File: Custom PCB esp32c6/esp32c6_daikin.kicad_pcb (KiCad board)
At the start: 2 copper layers, 31.6 x 19.8 mm, 31 parts, among them J2 Conn_01x07, Q1 BSS138PS, U1 TPS562246, U2 WT0132C6-S5

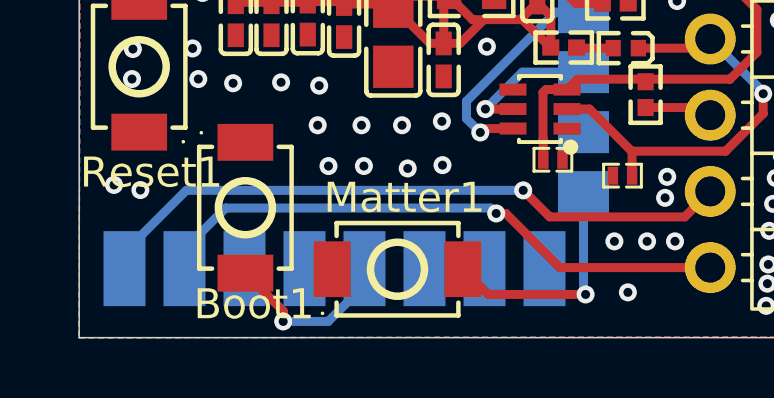
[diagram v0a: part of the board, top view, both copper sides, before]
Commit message: fix(pcb): move Boot1 via clear of the board edge
Sat 0.24mm from Edge.Cuts against a 0.5mm rule; edge routing tolerance
could nick it. A plain perpendicular retreat wasn't viable: the via sits
in a 1.05mm corridor between the U2 castellated pad row (0.6mm gaps
between 2.0mm-pitch pads) and the board edge, too tight to gain edge
clearance without shorting an adjacent pad. Relocated it into the same-net
column under U2 pad 12 (161.4,109.03 -> 164.11,108.6) and re-terminated
the two connected track segments there instead.

Also hardened refill.py to disable wx assert dialogs (wx.DisableAsserts())
so a stray pcbnew API nag (PCB_VIA::GetWidth called without a layer
argument, hit while probing pad geometry for this fix) can't block
future headless refill runs.
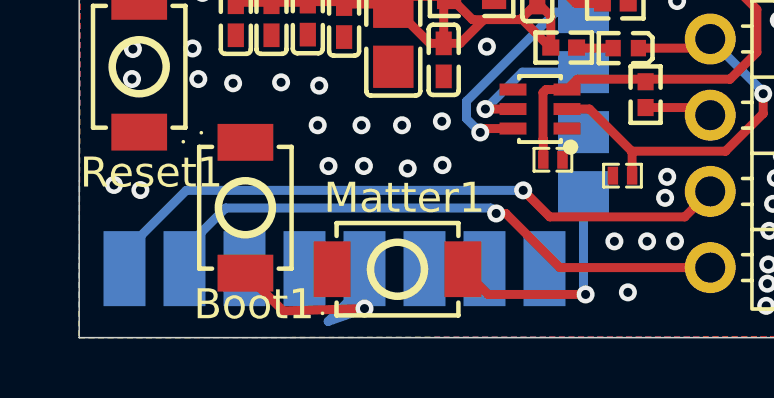
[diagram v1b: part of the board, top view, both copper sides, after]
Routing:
- net Net-(Boot1-A): track 5.89 -> 8.04 mm
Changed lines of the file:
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@@
 	)
 	(segment
-		(start 161.4 109.03)
+		(start 164.11 108.6)
 		(end 161.4 108.68)
 		(width 0.3)
@@
 	)
 	(via
-		(at 161.4 109.03)
+		(at 164.11 108.6)
 		(size 0.6)
 		(drill 0.3)
@@
 	(segment
 		(start 162.9 109.03)
-		(end 161.4 109.03)
+		(end 164.11 108.6)
 		(width 0.3)
 		(layer "B.Cu")

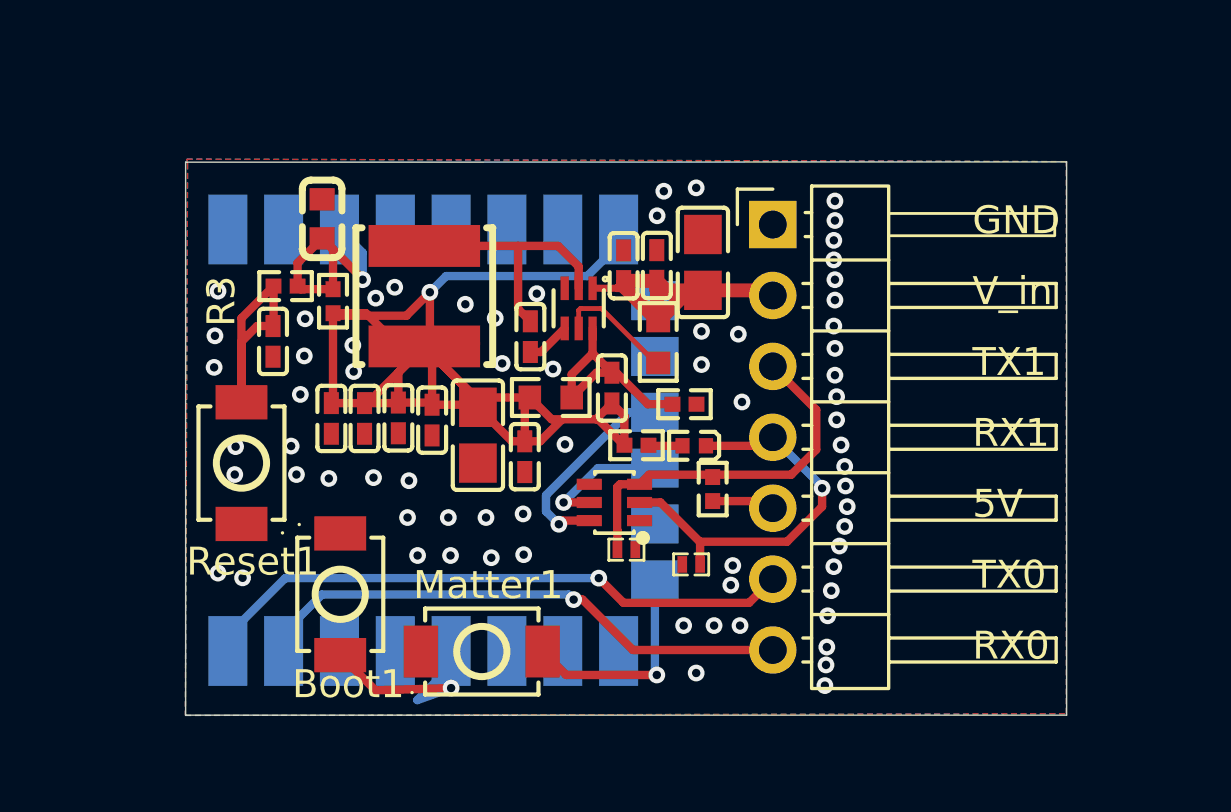
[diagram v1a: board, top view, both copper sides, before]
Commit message: fix(pcb): place/route 12V protection + S21 series resistors; remove old header
Sync + place + route the protection parts (F1 polyfuse, D5 SMF15A TVS,
R10/R11 S21 series resistors) into the PCB and route them to existing copper.

Old 7-pin J2 header is REMOVED in this commit rather than the connector
commit: its courtyard and THT pads span x[173.87..186.17] over the full
board height and occupy the only viable placement region for the protection
parts. Any parts-first layout with the header present is DRC-verified to
produce courtyard_overlap + shorting_items errors. The intermediate board
state therefore has no connector by design; commit B adds the JST-EH and
routes it to these parts. (Group A/B split was drawn on function, not
geometry; geometry forced the header removal here.)

Net changes: Net-(D4-K) -> /S21_RX_CONN, Net-(J2-Pin_3) -> Net-(Q1B-SP);
new /12V_IN (F1.2) and /S21_TX_CONN (R10.2) are single-pad until the
connector lands in commit B; R1.1 -> unconnected-(R1-Pad1). RX_CONN net was
re-bridged on B.Cu (old header pin4 had been its only junction). D5 oriented
pad1(cathode) -> V_in, pad2(anode) -> GND per the schematic pin map.

DRC (no parity, real rules): 0 unconnected, 0 errors, zone count 1.
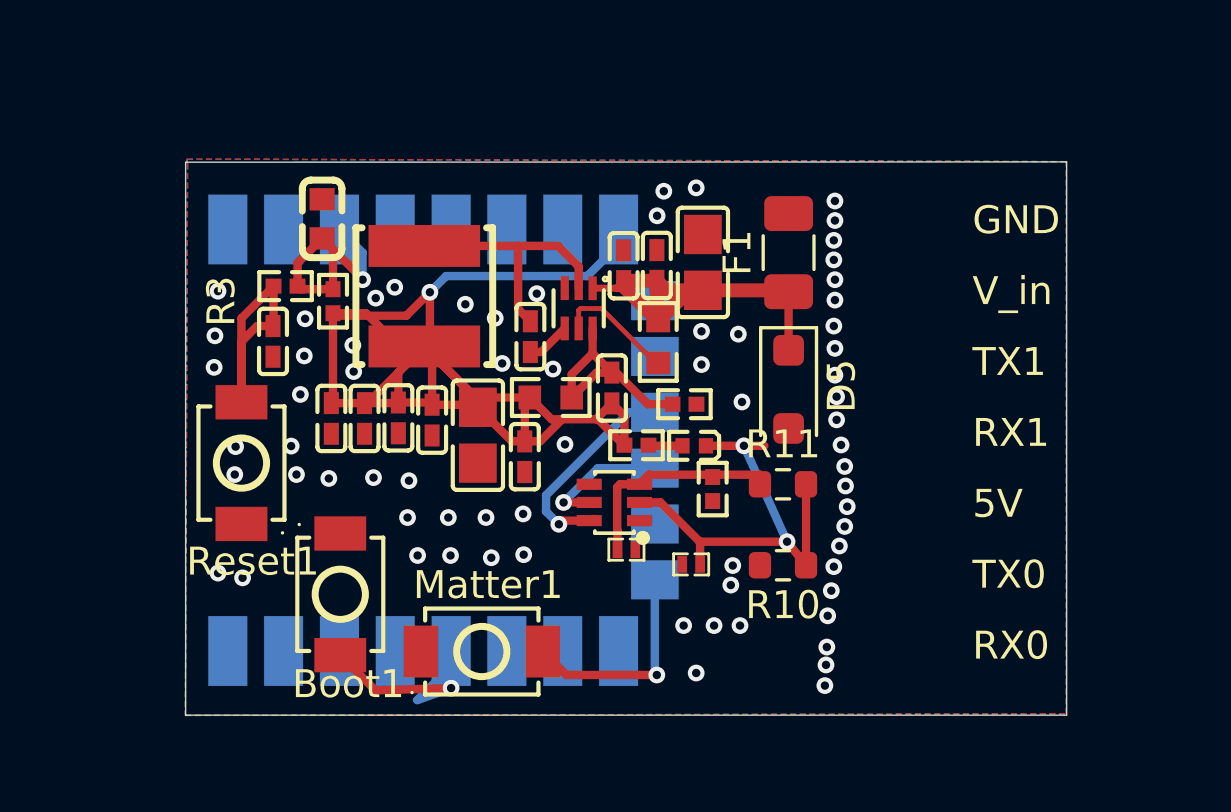
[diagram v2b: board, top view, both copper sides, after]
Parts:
- removed J2: Conn_01x07, Connector_PinHeader_2.54mm:PinHeader_1x07_P2.54mm_Horizontal
- added D5: D_SOD-123F, D_SOD-123F, F.Cu at (176.2, 97.9)
- added F1: Fuse_1206_3216Metric, Fuse_1206_3216Metric, F.Cu at (176.2, 93.0)
- added R10: R_0603_1608Metric, R_0603_1608Metric, F.Cu at (176.0, 104.2)
- added R11: R_0603_1608Metric, R_0603_1608Metric, F.Cu at (176.0, 101.3)
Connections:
- net Net-(D4-K) renamed /S21_RX_CONN
- R1 pad 1: Net-(J2-Pin_5) -> unconnected-(R1-Pad1)
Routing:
- net TX0: track 21.6 -> 0.00 mm, vias 1 -> 0
- net RX0: track 19.6 -> 0.00 mm, vias 1 -> 0
- net Net-(Q1B-SP): track 13.6 -> 7.89 mm
- net V_in: track 12.2 -> 14.8 mm
- net /S21_RX_CONN: track 14.2 -> 16.5 mm, vias 1 -> 2
- net Net-(J2-Pin_5): track 2.26 -> 0.00 mm

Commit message: feat(pcb): JST-EH connector placement and routing
Add the 5-pin JST-EH (S5B-EH horizontal) J2 on the right board edge, housing
and keying facing off-board, pin1 at top. Route to the protection parts placed
in commit A: J2.4->F1 (12V_IN, F.Cu), J2.2->R10 (S21_TX_CONN, B.Cu w/ one
F.Cu via-hop over RX), J2.3->S21_RX_CONN (B.Cu), J2.5->GND (F.Cu pour); J2.1 NC.

Removed 17 GND stitching vias from the connector rework region (x177.7-178.5,
y90.5-104) that formed a wall between the connector pins and the protection
parts. GND stays fully connected via the continuous F.Cu pour + the remaining
stitching vias (DRC unconnected==0 confirms).

Removed 7 stale old-header silk pin labels (GND/V_in/TX1/RX1/5V/TX0/RX0) that
sat over the new connector with the wrong pinout - a wiring hazard.

Synced footprint metadata for schematic parity: set correct library-qualified
FPID, Value, LCSC and Description on the 5 new footprints (F1/D5/R10/R11/J2),
and synced the LCSC field on 7 existing footprints (D2/D3/D4/Q1/R1/R2/U2) that
were missing it pre-Task-8 (Task 5-7 added LCSC to symbols, not footprints).

DRC (with --schematic-parity, real DRU/rules): 0 unconnected, 0 errors,
0 parity mismatches, zone count 1.
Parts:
- added J2: Conn_01x05, Connector_JST:JST_EH_S5B-EH_1x05_P2.50mm_Horizontal, F.Cu at (180.5, 94.5)
- D5: value D_SOD-123F -> SMF15A 15V; footprint D_SOD-123F -> Diode_SMD:D_SOD-123F
- F1: value Fuse_1206_3216Metric -> 250mA-hold 1206; footprint Fuse_1206_3216Metric -> Fuse:Fuse_1206_3216Metric
- R10, R11: value R_0603_1608Metric -> 220R; footprint R_0603_1608Metric -> Resistor_SMD:R_0603_1608Metric
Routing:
- net /12V_IN: track 0.00 -> 16.4 mm
- net /S21_TX_CONN: track 0.00 -> 10.2 mm, vias 0 -> 3
- net /S21_RX_CONN: track 16.5 -> 22.3 mm
- net GND: vias 69 -> 52
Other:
- board text removed: "5V"
- board text removed: "GND"
- board text removed: "RX0"
- board text removed: "RX1"
- board text removed: "TX0"
- board text removed: "TX1"
- board text removed: "V_in"

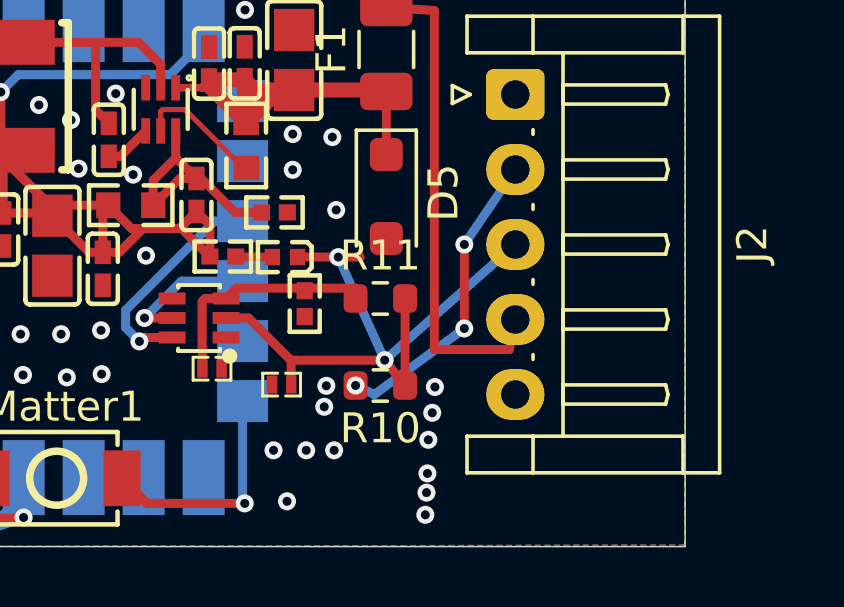
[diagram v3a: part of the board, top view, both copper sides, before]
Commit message: fix(sch+pcb): separate the two S21 signal nets merged by the JST-EH swap
The Task-6 JST-EH connector swap merged two S21 nets into one, tying
J2 pin 2 (aircon Tx) and J2 pin 3 (aircon Rx) together through R10 (220R)
and feeding the ESP's TX back into its RX front end. A single wire carrying
the /S21_RX_CONN label at the R10.1 row shorted J2.3, R11.2, and the
Q1.2/D3/D4 gate cluster onto one 6-node net.

This restores the Task-5 (commit 2981aef) two-net split, adapted to the new
JST-EH pin numbers:
  - /S21_TX_CORE (new label; was Net-(D4-K)) = {R10.1, Q1.2, D3.2, D4.1}
  - /S21_RX_CONN (reduced to)                = {J2.3, R11.2}
J2.2 and J2.3 now share no path except through the intended full front end.

Schematic: split the merge wire into two electrically separate wires and
added the S21_TX_CORE label; the four nets are netlist-verified (kicad-cli
export) with exactly the target node sets. ERC unchanged at 16 errors.

PCB: created net /S21_TX_CORE, reassigned pads R10.1/Q1.2/D3.2/D4.1 and
their cluster copper to it, deleted the two bridge tracks (R11.2->R10.1
vertical on F.Cu and J2.3->hub on B.Cu), and routed a new R11.2->J2.3 RX
path (F.Cu stub + via + B.Cu run under the 12V/TX columns). DRC clean:
0 unconnected, 0 errors, 0 schematic-parity mismatches, 1 zone.

refill.py: corrected the wx assert-suppression guard order (DisableAsserts
after importing pcbnew, with a wx.App) so refills no longer raise dialogs.
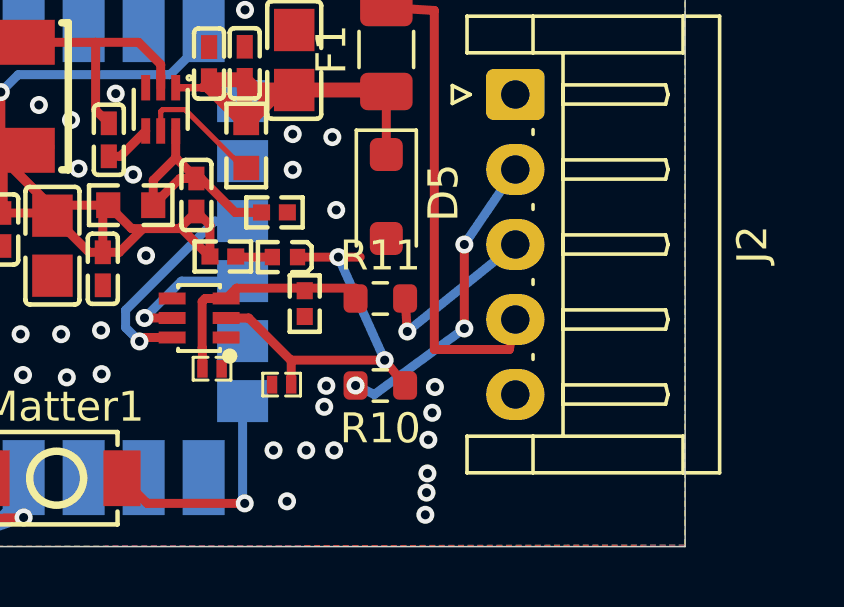
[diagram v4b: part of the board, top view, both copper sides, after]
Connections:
- D3 pad 2: /S21_RX_CONN -> /S21_TX_CORE
- D4 pad 1: /S21_RX_CONN -> /S21_TX_CORE
- Q1 pad 2: /S21_RX_CONN -> /S21_TX_CORE
- R10 pad 1: /S21_RX_CONN -> /S21_TX_CORE
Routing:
- net /S21_RX_CONN: track 22.3 -> 5.73 mm, vias 2 -> 1
- net /S21_TX_CORE: track 0.00 -> 13.6 mm, vias 0 -> 2
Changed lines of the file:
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@@
 			(size 0.51 0.55)
 			(layers "F.Cu" "F.Mask" "F.Paste")
-			(net "/S21_RX_CONN")
+			(net "/S21_TX_CORE")
 			(pinfunction "K_1")
 			(pintype "passive")
@@
 			(size 0.4 0.9)
 			(layers "F.Cu" "F.Mask" "F.Paste")
-			(net "/S21_RX_CONN")
+			(net "/S21_TX_CORE")
 			(pinfunction "GN_2")
 			(pintype "input")
@@
 			(size 0.35 0.6)
 			(layers "F.Cu" "F.Mask" "F.Paste")
-			(net "/S21_RX_CONN")
+			(net "/S21_TX_CORE")
 			(pintype "passive")
 			(teardrops
@@
 			(layers "F.Cu" "F.Mask" "F.Paste")
 			(roundrect_rratio 0.25)
-			(net "/S21_RX_CONN")
+			(net "/S21_TX_CORE")
 		)
 		(pad "2" smd roundrect
@@
 	)
 	(segment
-		(start 173.24 99.92)
-		(end 175.33 99.92)
-		(width 0.3)
-		(layer "F.Cu")
-		(net "/S21_RX_CONN")
-	)
-	(segment
-		(start 173.015 103.355)
-		(end 176.145 103.355)
-		(width 0.3)
-		(layer "F.Cu")
-		(net "/S21_RX_CONN")
-	)
-	(segment
 		(start 176.825 101.3)
-		(end 176.825 104.2)
-		(width 0.3)
-		(layer "F.Cu")
-		(net "/S21_RX_CONN")
-	)
-	(segment
-		(start 170.86 101.95)
-		(end 171.61 101.95)
+		(end 176.9 102.4)
 		(width 0.3)
 		(layer "F.Cu")
 		(net "/S21_RX_CONN")
 	)
-	(segment
-		(start 176.825 104.2)
-		(end 176.145 103.355)
-		(width 0.3)
-		(layer "F.Cu")
-		(net "/S21_RX_CONN")
-	)
-	(segment
-		(start 171.61 101.95)
-		(end 173.015 103.355)
-		(width 0.3)
-		(layer "F.Cu")
-		(net "/S21_RX_CONN")
-	)
-	(segment
-		(start 173.03 104.17)
-		(end 173.03 103.37)
-		(width 0.3)
-		(layer "F.Cu")
-		(net "/S21_RX_CONN")
-	)
-	(segment
-		(start 173.03 103.37)
-		(end 173.015 103.355)
-		(width 0.3)
-		(layer "F.Cu")
-		(net "/S21_RX_CONN")
-	)
-	(via
-		(at 176.145 103.355)
-		(size 0.6)
-		(drill 0.3)
-		(layers "F.Cu" "B.Cu")
-		(net "/S21_RX_CONN")
-	)
 	(via
-		(at 174.6 99.92)
+		(at 176.9 102.4)
 		(size 0.6)
 		(drill 0.3)
@@
 	)
 	(segment
-		(start 174.6 99.92)
-		(end 176.145 103.355)
-		(width 0.3)
-		(layer "B.Cu")
-		(net "/S21_RX_CONN")
-	)
-	(segment
-		(start 180.5 99.5)
-		(end 176.145 103.355)
+		(start 176.9 102.4)
+		(end 180.5 99.5)
 		(width 0.3)
 		(layer "B.Cu")
@@
 	)
 	(segment
+		(start 173.24 99.92)
+		(end 175.33 99.92)
+		(width 0.3)
+		(layer "F.Cu")
+		(net "/S21_TX_CORE")
+	)
+	(segment
+		(start 173.015 103.355)
+		(end 176.145 103.355)
+		(width 0.3)
+		(layer "F.Cu")
+		(net "/S21_TX_CORE")
+	)
+	(segment
+		(start 170.86 101.95)
+		(end 171.61 101.95)
+		(width 0.3)
+		(layer "F.Cu")
+		(net "/S21_TX_CORE")
+	)
+	(segment
+		(start 176.825 104.2)
+		(end 176.145 103.355)
+		(width 0.3)
+		(layer "F.Cu")
+		(net "/S21_TX_CORE")
+	)
+	(segment
+		(start 171.61 101.95)
+		(end 173.015 103.355)
+		(width 0.3)
+		(layer "F.Cu")
+		(net "/S21_TX_CORE")
+	)
+	(segment
+		(start 173.03 104.17)
+		(end 173.03 103.37)
+		(width 0.3)
+		(layer "F.Cu")
+		(net "/S21_TX_CORE")
+	)
+	(segment
+		(start 173.03 103.37)
+		(end 173.015 103.355)
+		(width 0.3)
+		(layer "F.Cu")
+		(net "/S21_TX_CORE")
+	)
+	(via
+		(at 176.145 103.355)
+		(size 0.6)
+		(drill 0.3)
+		(layers "F.Cu" "B.Cu")
+		(net "/S21_TX_CORE")
+	)
+	(via
+		(at 174.6 99.92)
+		(size 0.6)
+		(drill 0.3)
+		(layers "F.Cu" "B.Cu")
+		(net "/S21_TX_CORE")
+	)
+	(segment
+		(start 174.6 99.92)
+		(end 176.145 103.355)
+		(width 0.3)
+		(layer "B.Cu")
+		(net "/S21_TX_CORE")
+	)
+	(segment
